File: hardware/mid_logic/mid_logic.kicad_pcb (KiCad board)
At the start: 2 copper layers, 52 x 52 mm, 28 parts, among them J2 J_STK_A, J3 J_STK_B, J4 RS485 A/B/GND, J5 EXP P6/P7, Q2 BC847, SW1 RESET, SW2 BOOT, U1 ESP32-S3-WROOM-1-N16R8, U2 MAX3485, U3 PCF8574

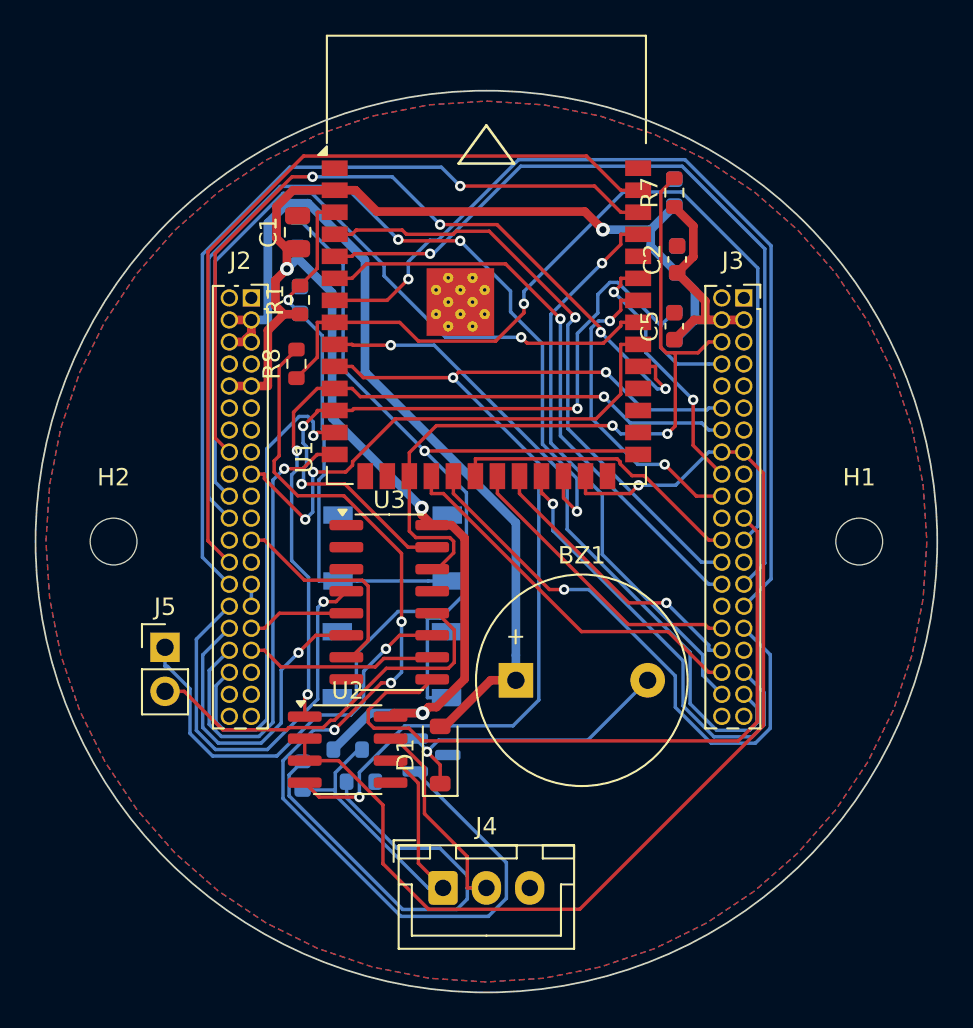
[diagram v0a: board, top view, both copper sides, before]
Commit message: Mid: Masse-Stichbahnen importiert, Zonen neu gefuellt
Erste GND-Runde des Iterators: offene PGND-Paare von 24 auf 12
reduziert (687 Wires, 62 Vias importiert). Der Iterator laeuft weiter;
die restlichen Paare (verwaiste Pads hinter parallelen Diagonalbahnen
und Pour-Inseln) sind Gegenstand der naechsten Runden.

Co-Authored-By: Claude Fable 5 <noreply@anthropic.com>
Claude-Session: https://claude.ai/code/session_017FTFDJW9R41k2WFeDRNE3w
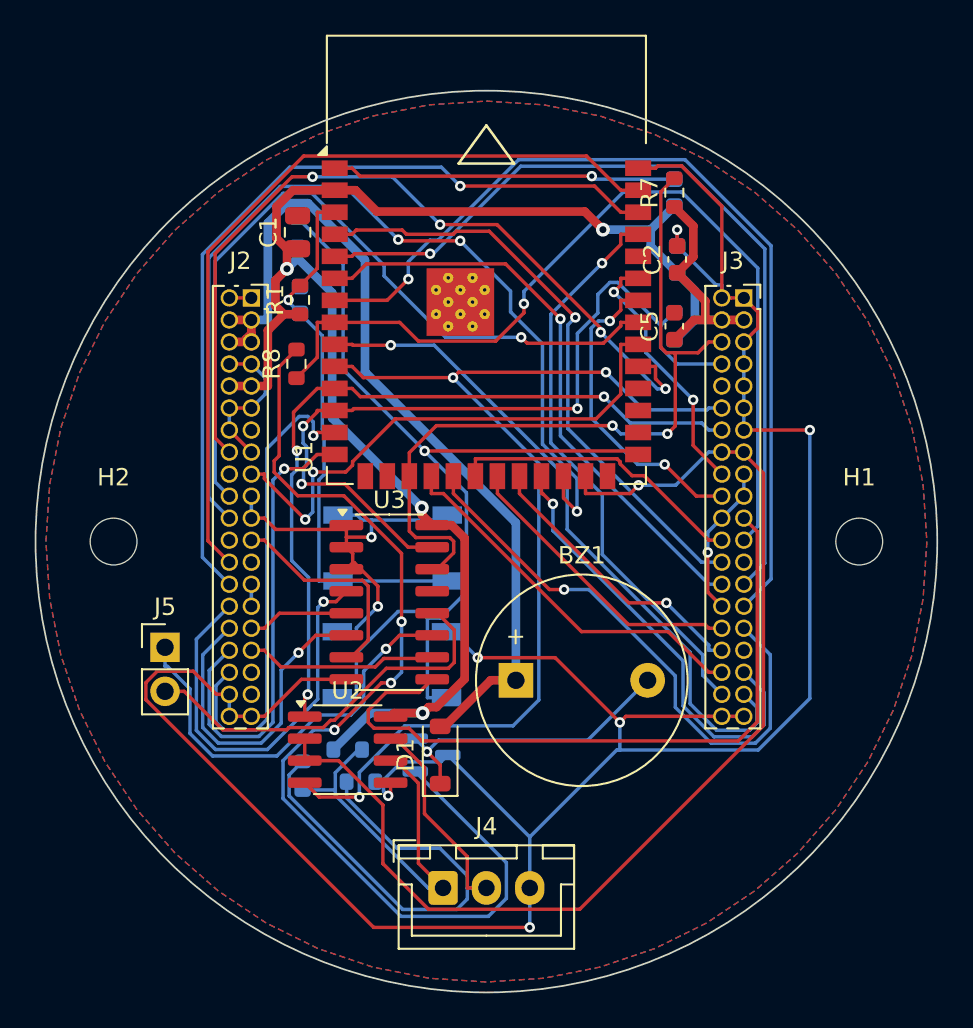
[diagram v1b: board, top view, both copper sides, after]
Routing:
- net PGND: track 0.00 -> 223.6 mm, vias 0 -> 10

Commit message: GND-Stitching-Werkzeug; Mid: Wandnetze fuer finalen GND-Lauf gerippt
tools/gnd_stitch.py setzt Stitching-Vias per Polygon-Containment
(Punkt mit Randabstand in beiden Lagen-Fragmenten). Vier Fragmente auf
dem Mid-Board wurden so verbunden. Die verbliebenen Orphan-Pins sitzen
hinter wenigen Signal-Waenden (USB_DP/DN-Verticals an der J2-Spalte,
BTN/RADAR/RS485-Verticals an J3) - innerhalb des 1,27-mm-Rasters mit
1,0-mm-Pads ist zwischen den Reihen prinzipiell kein Platz (0,635 mm
Abstand bei 0,75 mm Bedarf). Diese 12 Netze sind zusammen mit allen
PGND-Bahnen aufgerissen; Freerouting legt sie gerade gemeinsam neu.
Insel-Modus zurueck auf Flaechen-Schwelle (ALWAYS loeschte Fragmente,
die nur ein Pad beruehrten, und riss damit neue Luecken).

Co-Authored-By: Claude Fable 5 <noreply@anthropic.com>
Claude-Session: https://claude.ai/code/session_017FTFDJW9R41k2WFeDRNE3w
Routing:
- net PGND: track 223.6 -> 229.5 mm, vias 10 -> 14

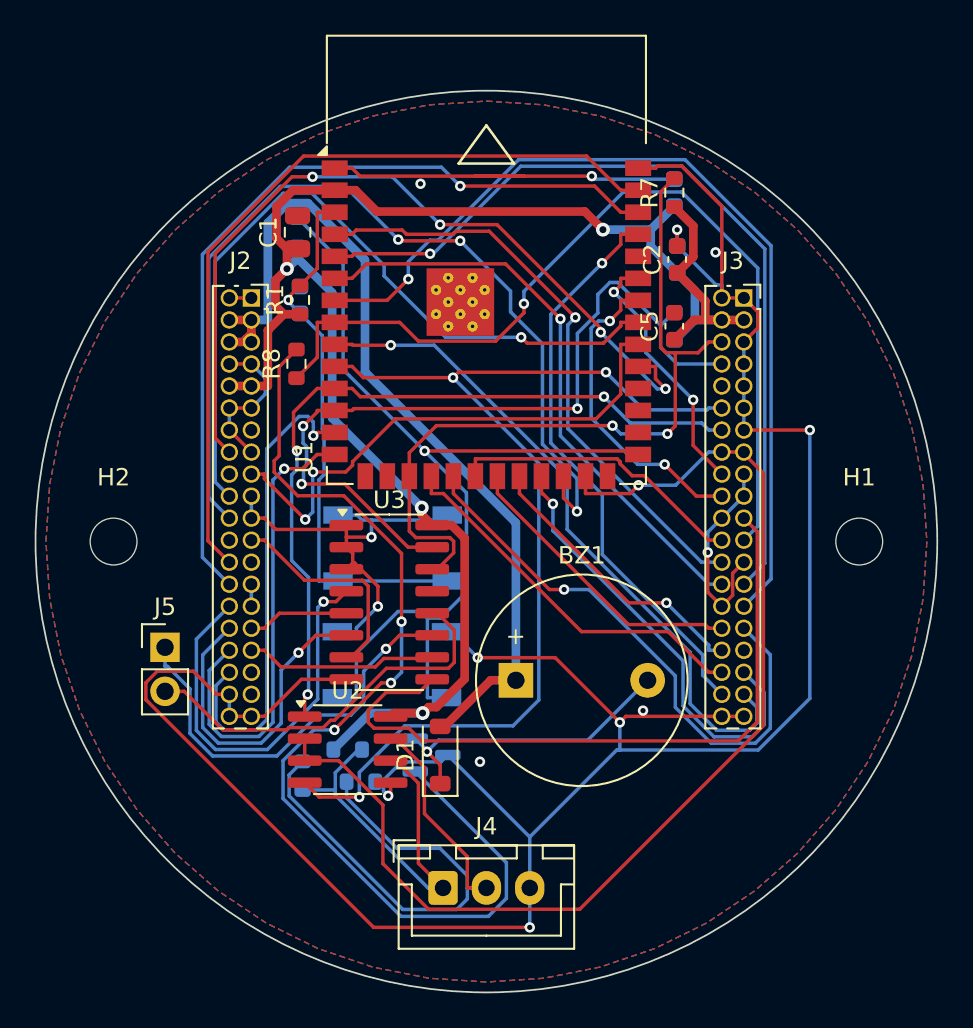
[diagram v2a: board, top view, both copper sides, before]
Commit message: Bottom: Standard-Vias und -Clearance fuer Leistungsklassen
Die 0,8er-Vias mit 0,2er-Clearance passen nicht in die Schluchten
zwischen den FET-Pads - die letzten ~50 Verbindungen blieben ueber
mehrere Stunden Autorouting dauerhaft offen. Jetzt 0,6/0,3-Vias und
0,15er-Clearance auch fuer PWR/RAIL auf dem Bottom-Board (2-3 A je
Via, ausreichend fuer Laufstrom und kurze Transienten; Handnacharbeit
der Leistungspfade vor Fertigung bleibt Pflicht per docs/05).
Bottom-Fortsetzungslauf mit den entspannten Regeln laeuft. Zudem
Bottom-Stand nach erster Fortsetzung (62 -> 53 offen) und Mid-Stand
nach finalem Wandnetz-Lauf (J3-25/33-Kette per Stich angebunden,
7 Paare offen, Iterator laeuft) uebernommen.

Co-Authored-By: Claude Fable 5 <noreply@anthropic.com>
Claude-Session: https://claude.ai/code/session_017FTFDJW9R41k2WFeDRNE3w
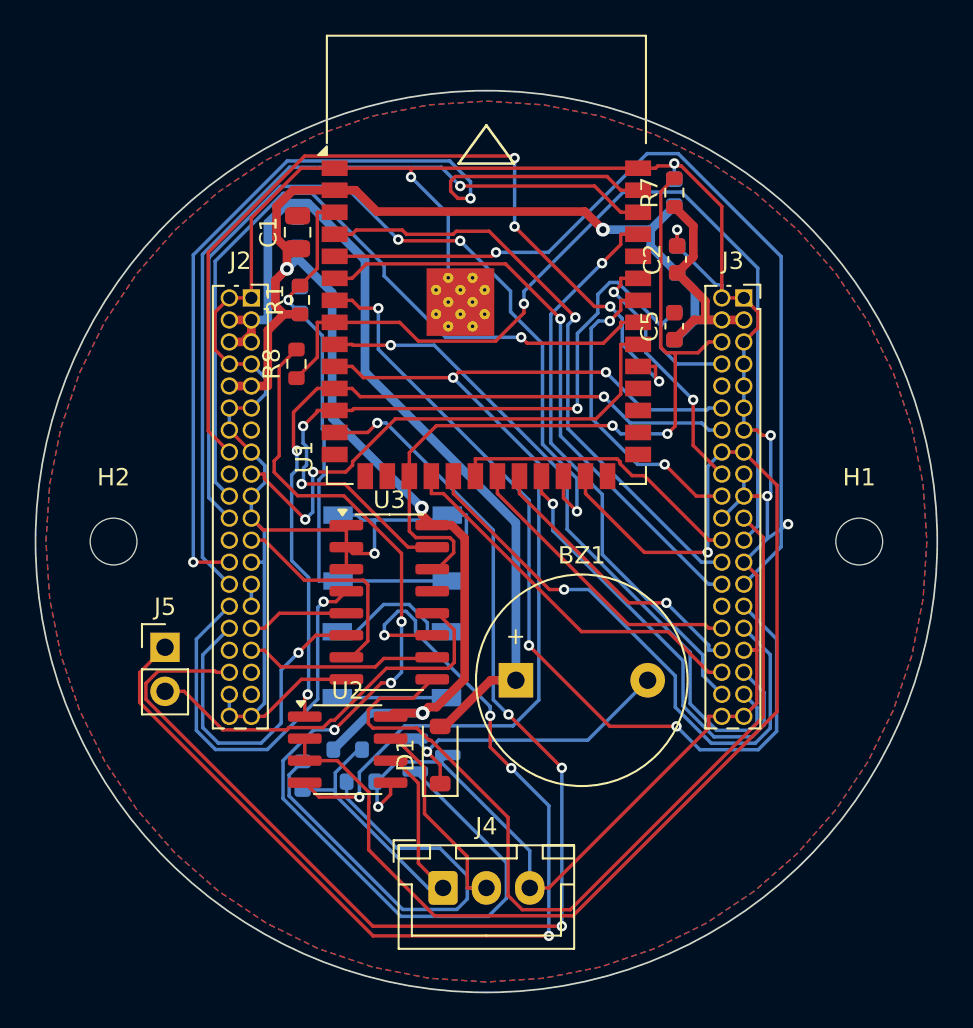
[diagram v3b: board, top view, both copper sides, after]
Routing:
- net ESP_BOOT: track 55.5 -> 6.30 mm, vias 1 -> 0
- net USB_DN: track 27.8 -> 71.9 mm, vias 1 -> 4
- net EXP_P6: track 24.1 -> 60.0 mm, vias 1 -> 4
- net USB_DP: track 27.2 -> 0.00 mm, vias 1 -> 0
- net PGND: track 229.5 -> 212.0 mm, vias 14 -> 8
- net RADAR_INT: track 40.5 -> 51.6 mm
- net RS485_DIR: track 65.2 -> 71.7 mm
- net I_SENSE1: track 46.3 -> 52.6 mm, vias 0 -> 2
- net M1_INA: track 47.3 -> 50.9 mm
- net BTN2: track 48.8 -> 50.4 mm
- net BTN4: track 52.6 -> 51.0 mm, vias 1 -> 3

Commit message: Mid: USB_DP-Handroute, J3-30-Anbindung, ESP_BOOT-Blocker gerippt
USB_DP laeuft jetzt von U1-14 durch den (nach dem Wandnetz-Rip freien)
Innenkorridor an J2 vorbei um das obere Verbinderende zu J2-34.
J3-30 steigt innen-links aus dem Steckerraster aus und haengt per Via
an beiden Masseflaechen. Fuer die letzte offene Verbindung (ESP_BOOT
quer uebers Board) sind die vier querenden Wandnetze (DISP_RST,
DISP_BL, EXP_P6, UART485_TX) aufgerissen; Freerouting legt sie
zusammen mit ESP_BOOT gerade neu. Reste des vorherigen Versuchs
(Via/Stub am Rand, 3-um-Fragment) entfernt.

Co-Authored-By: Claude Fable 5 <noreply@anthropic.com>
Claude-Session: https://claude.ai/code/session_017FTFDJW9R41k2WFeDRNE3w
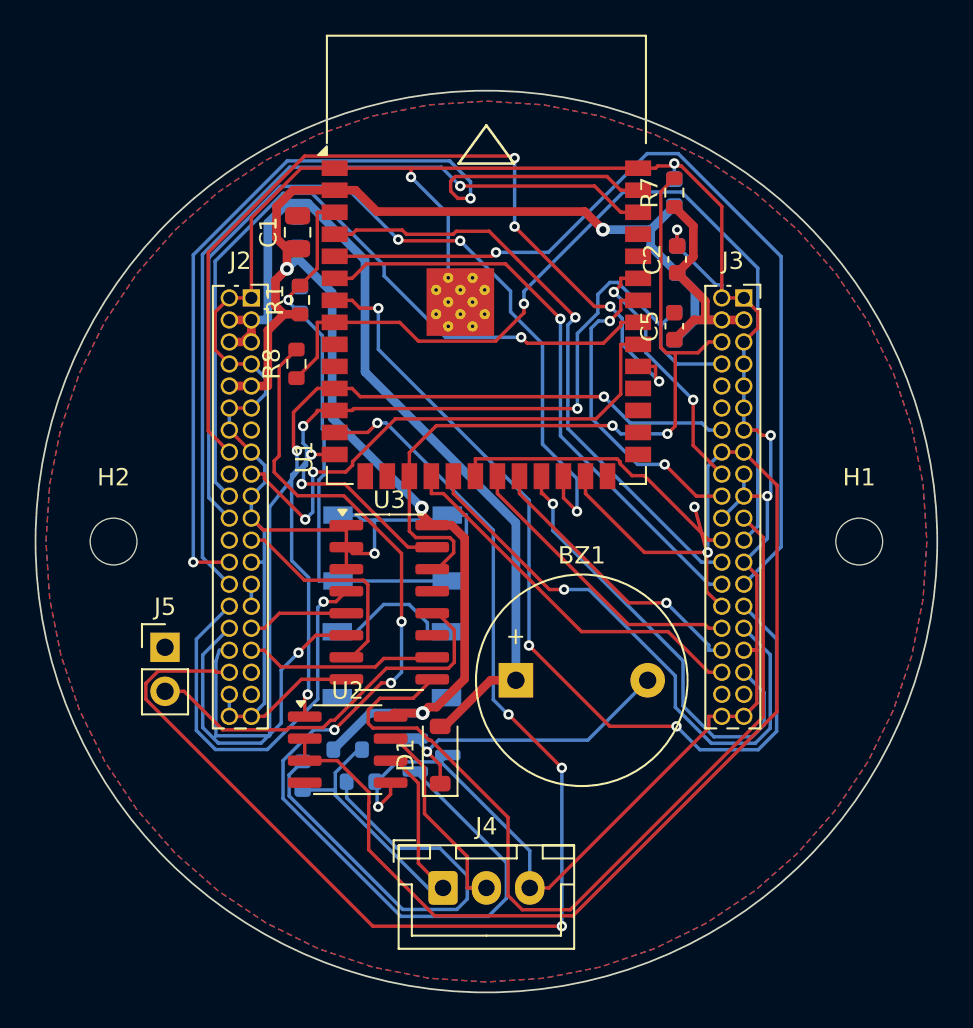
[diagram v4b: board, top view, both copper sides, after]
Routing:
- net UART485_TX: track 61.3 -> 0.00 mm, vias 3 -> 0
- net EXP_P6: track 60.0 -> 0.00 mm, vias 4 -> 0
- net DISP_RST: track 39.2 -> 0.00 mm, vias 1 -> 0
- net DISP_BL: track 33.3 -> 0.00 mm, vias 1 -> 0
- net USB_DP: track 0.00 -> 27.0 mm, vias 0 -> 1
- net ESP_BOOT: track 6.30 -> 0.00 mm
- net PGND: track 212.0 -> 216.7 mm

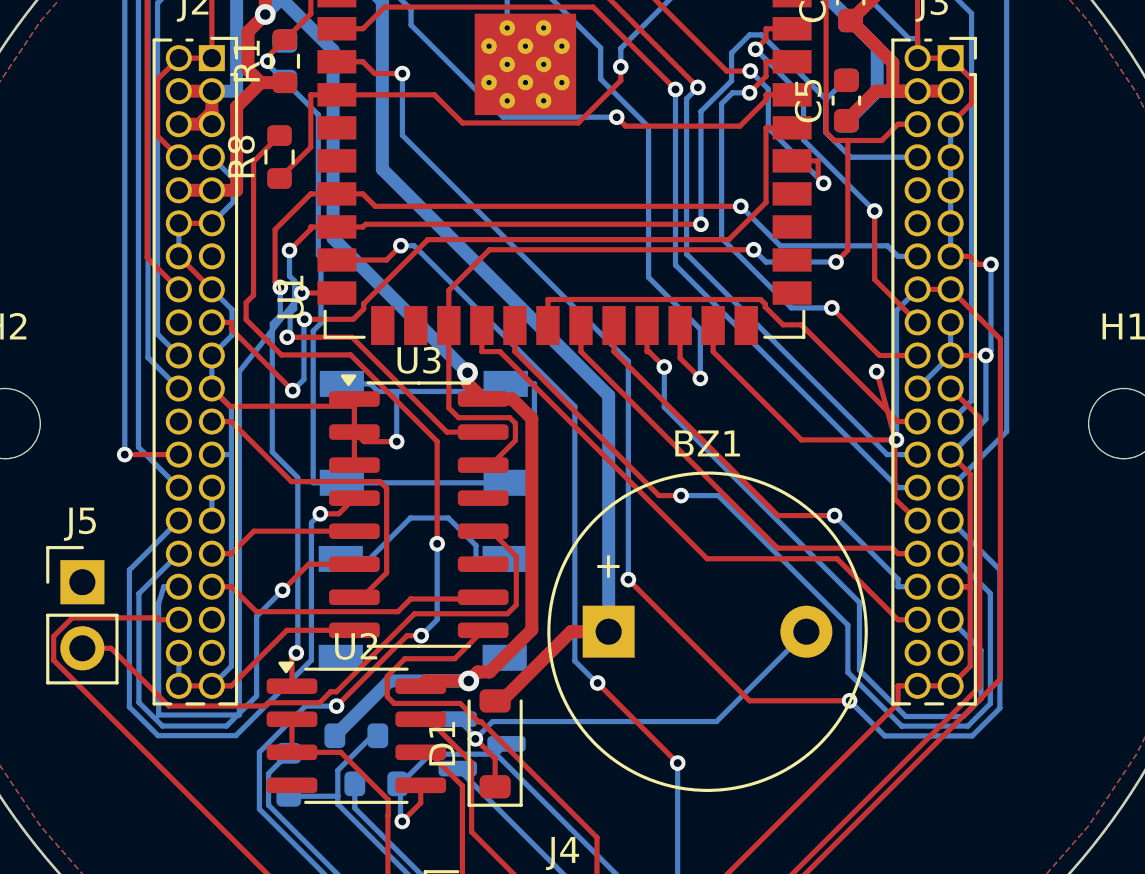
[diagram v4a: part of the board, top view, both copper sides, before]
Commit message: Mid: Zwischenstand vor frischem Komplett-Lauf
Die Handrouten fuer USB_DP/J3-30 kollidierten mit zwischenzeitlich
umgelegten Netzen (TRIP_RST u.a.) und sind entfernt; die inkrementell
gewachsene Verdrahtung oszilliert im Router (USB_DP, DISP_BL/RST,
EXP_P6 dauerhaft offen). Ein frischer Komplett-Lauf der Pipeline
laeuft - der erste solche Lauf kam seinerzeit bis auf eine offene
Verbindung.

Co-Authored-By: Claude Fable 5 <noreply@anthropic.com>
Claude-Session: https://claude.ai/code/session_017FTFDJW9R41k2WFeDRNE3w
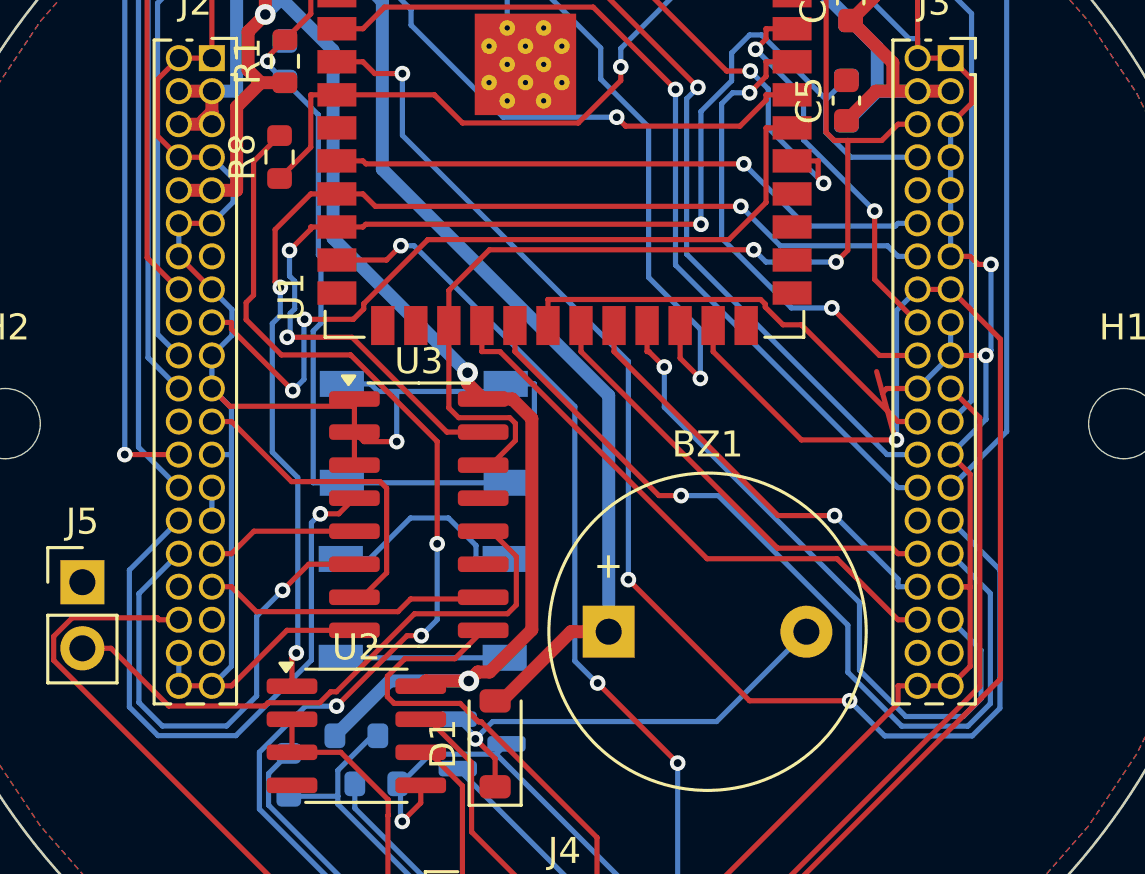
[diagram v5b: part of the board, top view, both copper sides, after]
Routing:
- net USB_DP: track 27.0 -> 0.00 mm, vias 1 -> 0
- net UART485_TX: track 0.00 -> 23.4 mm, vias 0 -> 1
- net ESP_BOOT: track 0.00 -> 6.30 mm
- net PGND: track 216.7 -> 214.6 mm, vias 8 -> 7
